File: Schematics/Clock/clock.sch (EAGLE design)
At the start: 13 parts, among them IC1 NE555N

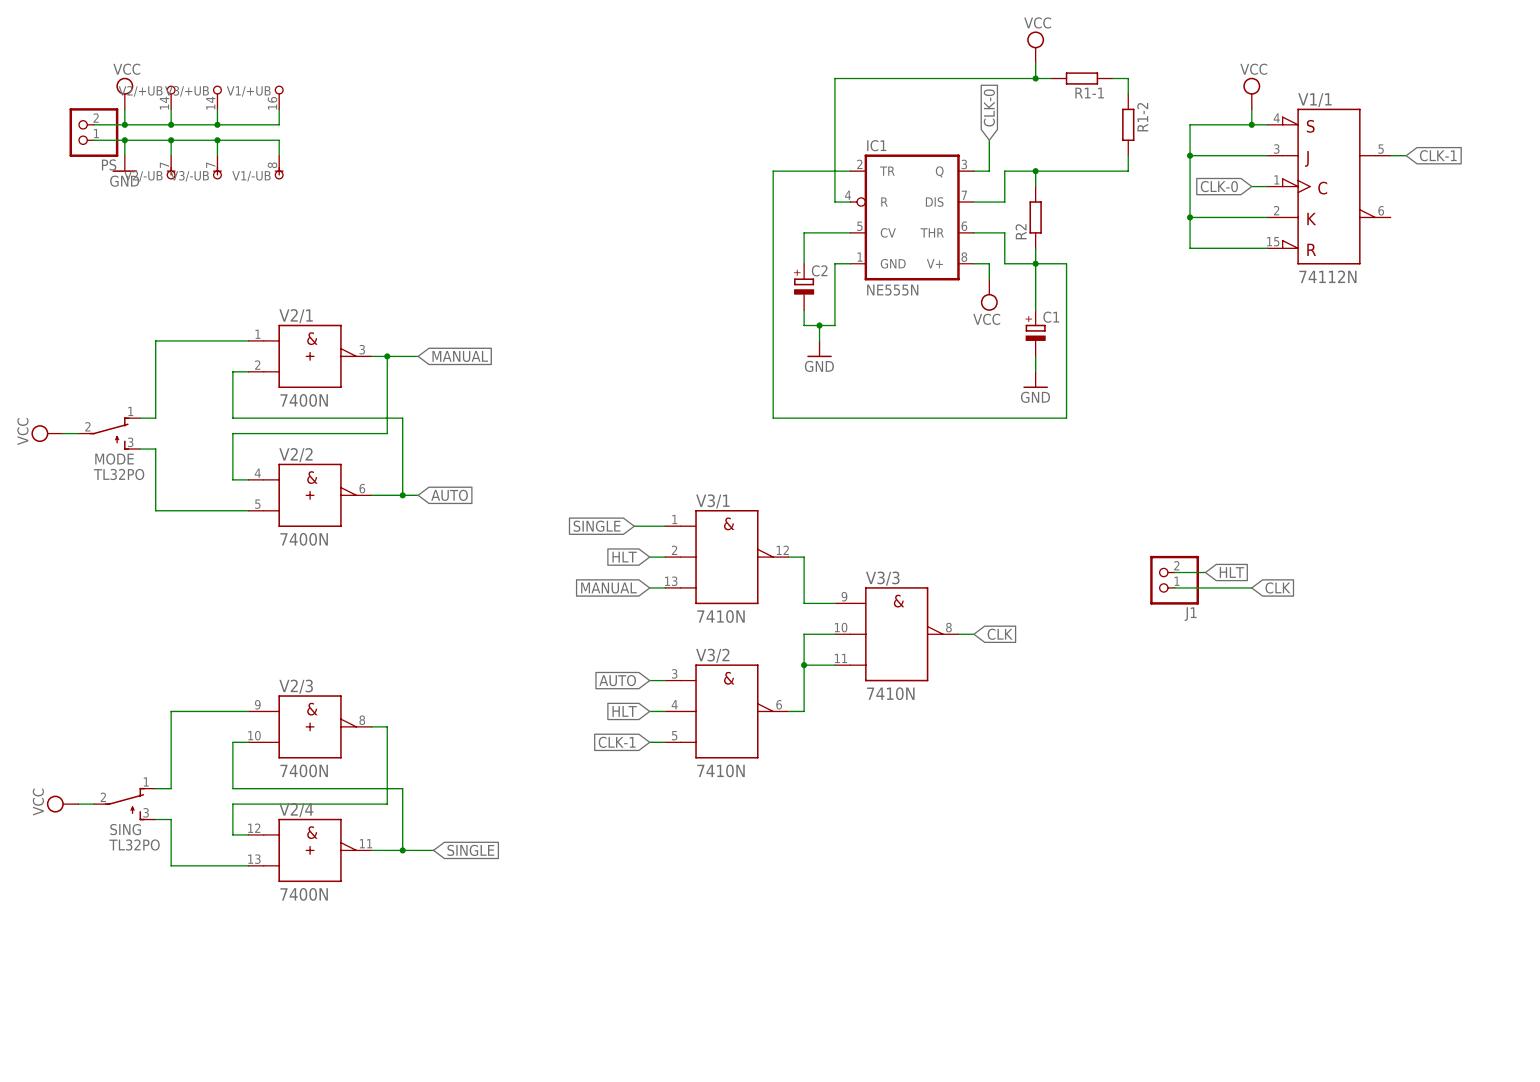
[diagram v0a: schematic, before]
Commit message: Added pull down resisotors to NAND gates. Maybe 'single' will be button.
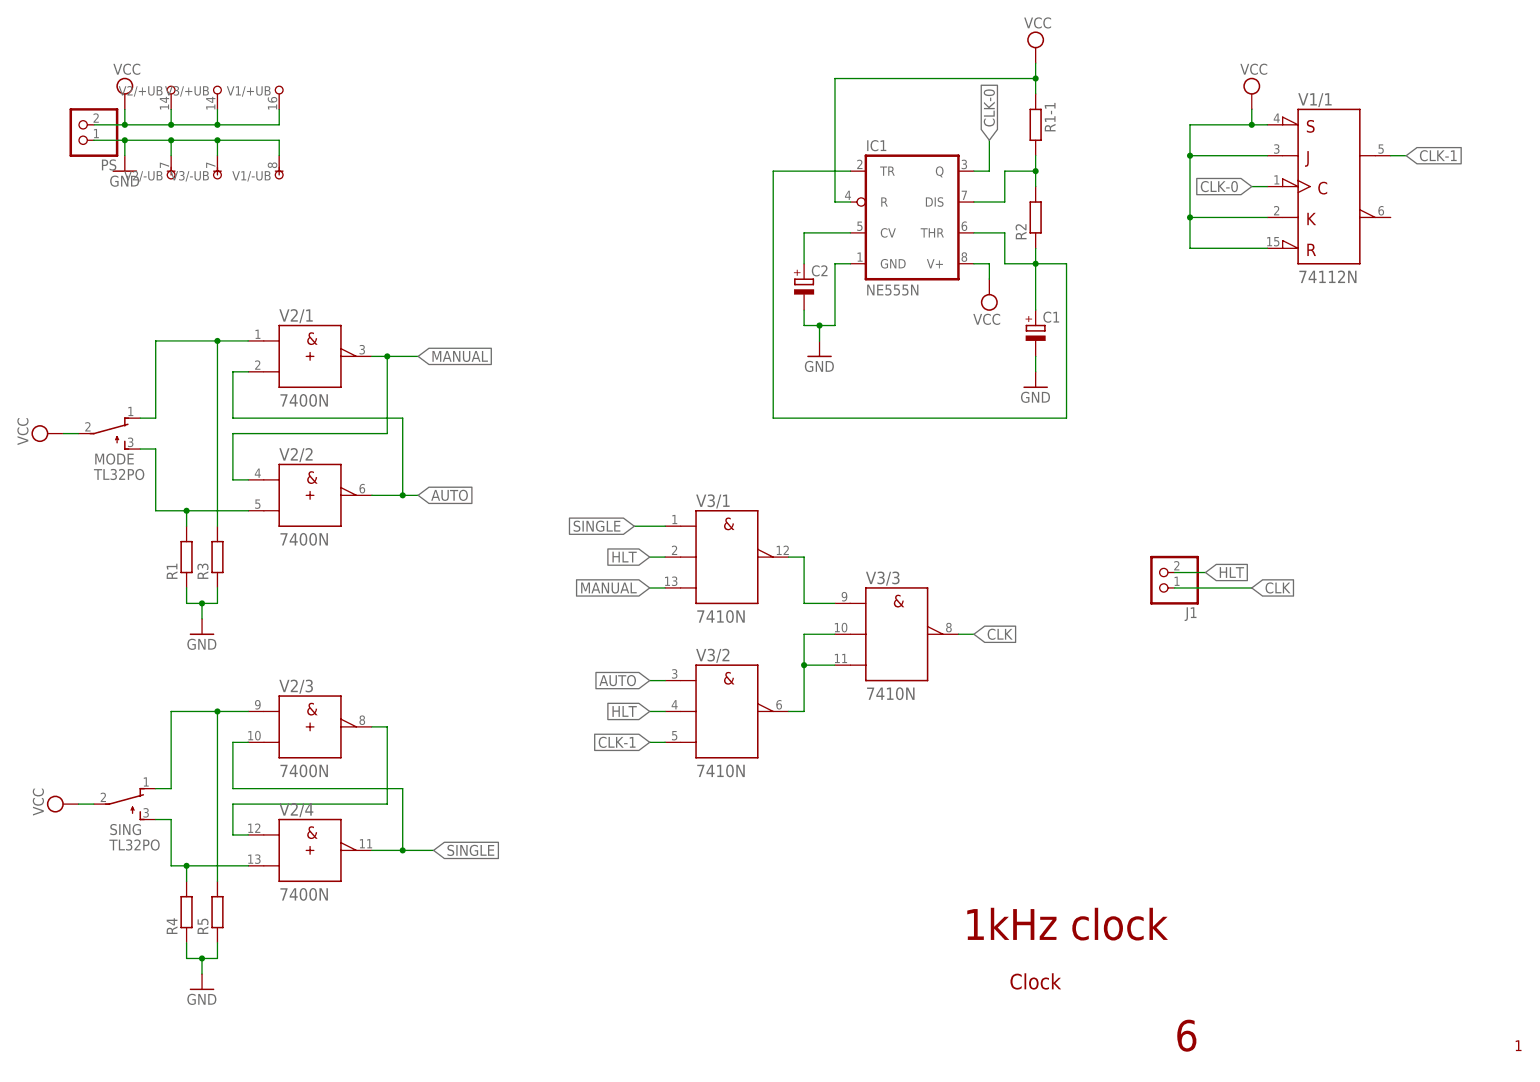
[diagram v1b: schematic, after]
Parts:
- removed R1-2: (no value), rcl:R-EU_0207/10
- added R1, R3, R4, R5: (no value), rcl:R-EU_0204/7
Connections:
- removed net N$4: R1-1.1, R1-2.1
- net GND: now also R1.1, R3.1, R4.1, R5.1
- net N$11: now also R5.2
- net N$12: now also R4.2
- net N$2: now also R1-1.2; no longer R1-2.2
- net N$7: now also R3.2
- net N$8: now also R1.2
- net VCC: now also R1-1.1; no longer R1-1.2
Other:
- note added: "1"
- note added: "1kHz clock"
- note added: "6"
- note added: "Clock"
- moved on the sheet: R1-1
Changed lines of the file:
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@@
 <part name="SUPPLY1" library="supply2" library_urn="urn:adsk.eagle:library:372" deviceset="VCC" device=""/>
 <part name="SUPPLY2" library="supply2" library_urn="urn:adsk.eagle:library:372" deviceset="VCC" device=""/>
-<part name="R1-2" library="rcl" library_urn="urn:adsk.eagle:library:334" deviceset="R-EU_" device="0207/10" package3d_urn="urn:adsk.eagle:package:23491/2"/>
 <part name="V1" library="74ttl-din" library_urn="urn:adsk.eagle:library:84" deviceset="74*112" device="N" package3d_urn="urn:adsk.eagle:package:922/2"/>
 <part name="SUPPLY3" library="supply2" library_urn="urn:adsk.eagle:library:372" deviceset="VCC" device=""/>
@@
 <part name="GND3" library="supply1" library_urn="urn:adsk.eagle:library:371" deviceset="GND" device=""/>
 <part name="J1" library="pinhead" library_urn="urn:adsk.eagle:library:325" deviceset="PINHD-1X2" device="" package3d_urn="urn:adsk.eagle:package:22435/2"/>
+<part name="R1" library="rcl" library_urn="urn:adsk.eagle:library:334" deviceset="R-EU_" device="0204/7" package3d_urn="urn:adsk.eagle:package:23498/2"/>
+<part name="R3" library="rcl" library_urn="urn:adsk.eagle:library:334" deviceset="R-EU_" device="0204/7" package3d_urn="urn:adsk.eagle:package:23498/2"/>
+<part name="R4" library="rcl" library_urn="urn:adsk.eagle:library:334" deviceset="R-EU_" device="0204/7" package3d_urn="urn:adsk.eagle:package:23498/2"/>
+<part name="R5" library="rcl" library_urn="urn:adsk.eagle:library:334" deviceset="R-EU_" device="0204/7" package3d_urn="urn:adsk.eagle:package:23498/2"/>
+<part name="GND4" library="supply1" library_urn="urn:adsk.eagle:library:371" deviceset="GND" device=""/>
+<part name="GND5" library="supply1" library_urn="urn:adsk.eagle:library:371" deviceset="GND" device=""/>
 </parts>
 <sheets>
 <sheet>
 <plain>
+<text x="259.08" y="7.62" size="1.778" layer="94">1</text>
+<text x="203.2" y="7.62" size="5.08" layer="94">6</text>
+<text x="176.022" y="17.78" size="2.54" layer="94">Clock</text>
+<text x="168.402" y="25.908" size="5.08" layer="94">1kHz clock</text>
 </plain>
 <instances>
@@
 <attribute name="LAST_DATE_TIME" x="175.26" y="1.27" size="2.54" layer="94"/>
 <attribute name="SHEET" x="248.92" y="1.27" size="2.54" layer="94"/>
-<attribute name="DRAWING_NAME" x="180.34" y="19.05" size="2.54" layer="94"/>
-</instance>
-<instance part="R1-1" gate="G$1" x="187.96" y="167.64" smashed="yes" rot="R180">
-<attribute name="NAME" x="191.77" y="166.1414" size="1.778" layer="95" rot="R180"/>
-<attribute name="VALUE" x="191.77" y="170.942" size="1.778" layer="96" rot="R180"/>
+</instance>
+<instance part="R1-1" gate="G$1" x="180.34" y="160.02" smashed="yes" rot="R270">
+<attribute name="NAME" x="181.8386" y="163.83" size="1.778" layer="95" rot="R270"/>
+<attribute name="VALUE" x="177.038" y="163.83" size="1.778" layer="96" rot="R270"/>
 </instance>
 <instance part="R2" gate="G$1" x="180.34" y="144.78" smashed="yes" rot="R90">
@@
 <attribute name="VALUE" x="174.625" y="128.905" size="1.778" layer="96" rot="R180"/>
 </instance>
-<instance part="R1-2" gate="G$1" x="195.58" y="160.02" smashed="yes" rot="R270">
-<attribute name="NAME" x="197.0786" y="163.83" size="1.778" layer="95" rot="R270"/>
-<attribute name="VALUE" x="192.278" y="163.83" size="1.778" layer="96" rot="R270"/>
-</instance>
 <instance part="V1" gate="/1" x="228.6" y="149.86" smashed="yes">
 <attribute name="NAME" x="223.52" y="163.195" size="2.032" layer="95"/>
@@
 <instance part="V1" gate="/-UB" x="55.88" y="152.4" smashed="yes" rot="R180">
 <attribute name="NAME" x="54.61" y="152.4" size="1.524" layer="95" rot="R180"/>
+</instance>
+<instance part="R1" gate="G$1" x="40.64" y="88.9" smashed="yes" rot="R90">
+<attribute name="NAME" x="39.1414" y="85.09" size="1.778" layer="95" rot="R90"/>
+<attribute name="VALUE" x="43.942" y="85.09" size="1.778" layer="96" rot="R90"/>
+</instance>
+<instance part="R3" gate="G$1" x="45.72" y="88.9" smashed="yes" rot="R90">
+<attribute name="NAME" x="44.2214" y="85.09" size="1.778" layer="95" rot="R90"/>
+<attribute name="VALUE" x="49.022" y="85.09" size="1.778" layer="96" rot="R90"/>
+</instance>
+<instance part="R4" gate="G$1" x="40.64" y="30.48" smashed="yes" rot="R90">
+<attribute name="NAME" x="39.1414" y="26.67" size="1.778" layer="95" rot="R90"/>
+<attribute name="VALUE" x="43.942" y="26.67" size="1.778" layer="96" rot="R90"/>
+</instance>
+<instance part="R5" gate="G$1" x="45.72" y="30.48" smashed="yes" rot="R90">
+<attribute name="NAME" x="44.2214" y="26.67" size="1.778" layer="95" rot="R90"/>
+<attribute name="VALUE" x="49.022" y="26.67" size="1.778" layer="96" rot="R90"/>
+</instance>
+<instance part="GND4" gate="1" x="43.18" y="76.2" smashed="yes">
+<attribute name="VALUE" x="40.64" y="73.66" size="1.778" layer="96"/>
+</instance>
+<instance part="GND5" gate="1" x="43.18" y="17.78" smashed="yes">
+<attribute name="VALUE" x="40.64" y="15.24" size="1.778" layer="96"/>
 </instance>
 </instances>
@@
 <wire x1="175.26" y1="147.32" x2="175.26" y2="152.4" width="0.1524" layer="91"/>
 <wire x1="175.26" y1="152.4" x2="180.34" y2="152.4" width="0.1524" layer="91"/>
-<wire x1="180.34" y1="152.4" x2="195.58" y2="152.4" width="0.1524" layer="91"/>
+<pinref part="R1-1" gate="G$1" pin="2"/>
+<wire x1="180.34" y1="154.94" x2="180.34" y2="152.4" width="0.1524" layer="91"/>
 <junction x="180.34" y="152.4"/>
-<pinref part="R1-2" gate="G$1" pin="2"/>
-<wire x1="195.58" y1="152.4" x2="195.58" y2="154.94" width="0.1524" layer="91"/>
 </segment>
 </net>
@@
 <wire x1="147.32" y1="147.32" x2="147.32" y2="167.64" width="0.1524" layer="91"/>
 <wire x1="147.32" y1="167.64" x2="180.34" y2="167.64" width="0.1524" layer="91"/>
-<pinref part="R1-1" gate="G$1" pin="2"/>
-<wire x1="180.34" y1="167.64" x2="182.88" y2="167.64" width="0.1524" layer="91"/>
 <pinref part="SUPPLY1" gate="G$1" pin="VCC"/>
 <wire x1="180.34" y1="170.18" x2="180.34" y2="167.64" width="0.1524" layer="91"/>
+<pinref part="R1-1" gate="G$1" pin="1"/>
+<wire x1="180.34" y1="165.1" x2="180.34" y2="167.64" width="0.1524" layer="91"/>
 <junction x="180.34" y="167.64"/>
 </segment>
@@
 <junction x="38.1" y="157.48"/>
 </segment>
+<segment>
+<pinref part="R1" gate="G$1" pin="1"/>
+<wire x1="40.64" y1="83.82" x2="40.64" y2="81.28" width="0.1524" layer="91"/>
+<wire x1="40.64" y1="81.28" x2="43.18" y2="81.28" width="0.1524" layer="91"/>
+<pinref part="R3" gate="G$1" pin="1"/>
+<wire x1="43.18" y1="81.28" x2="45.72" y2="81.28" width="0.1524" layer="91"/>
+<wire x1="45.72" y1="81.28" x2="45.72" y2="83.82" width="0.1524" layer="91"/>
+<pinref part="GND4" gate="1" pin="GND"/>
+<wire x1="43.18" y1="78.74" x2="43.18" y2="81.28" width="0.1524" layer="91"/>
+<junction x="43.18" y="81.28"/>
+</segment>
+<segment>
+<pinref part="R4" gate="G$1" pin="1"/>
+<wire x1="40.64" y1="25.4" x2="40.64" y2="22.86" width="0.1524" layer="91"/>
+<wire x1="40.64" y1="22.86" x2="43.18" y2="22.86" width="0.1524" layer="91"/>
+<pinref part="R5" gate="G$1" pin="1"/>
+<wire x1="43.18" y1="22.86" x2="45.72" y2="22.86" width="0.1524" layer="91"/>
+<wire x1="45.72" y1="22.86" x2="45.72" y2="25.4" width="0.1524" layer="91"/>
+<pinref part="GND5" gate="1" pin="GND"/>
+<wire x1="43.18" y1="20.32" x2="43.18" y2="22.86" width="0.1524" layer="91"/>
+<junction x="43.18" y="22.86"/>
+</segment>
 </net>
 <net name="CLK-0" class="0">
@@
 <wire x1="218.44" y1="149.86" x2="215.9" y2="149.86" width="0.1524" layer="91"/>
 <label x="215.9" y="149.86" size="1.778" layer="95" rot="R180" xref="yes"/>
-</segment>
-</net>
-<net name="N$4" class="0">
-<segment>
-<pinref part="R1-2" gate="G$1" pin="1"/>
-<wire x1="195.58" y1="165.1" x2="195.58" y2="167.64" width="0.1524" layer="91"/>
-<pinref part="R1-1" gate="G$1" pin="1"/>
-<wire x1="195.58" y1="167.64" x2="193.04" y2="167.64" width="0.1524" layer="91"/>
 </segment>
 </net>
@@
 <wire x1="33.02" y1="111.76" x2="35.56" y2="111.76" width="0.1524" layer="91"/>
 <wire x1="35.56" y1="111.76" x2="35.56" y2="124.46" width="0.1524" layer="91"/>
-<wire x1="35.56" y1="124.46" x2="50.8" y2="124.46" width="0.1524" layer="91"/>
+<wire x1="35.56" y1="124.46" x2="45.72" y2="124.46" width="0.1524" layer="91"/>
+<pinref part="R3" gate="G$1" pin="2"/>
+<wire x1="45.72" y1="124.46" x2="50.8" y2="124.46" width="0.1524" layer="91"/>
+<wire x1="45.72" y1="93.98" x2="45.72" y2="124.46" width="0.1524" layer="91"/>
+<junction x="45.72" y="124.46"/>
 </segment>
 </net>
@@
 <wire x1="33.02" y1="106.68" x2="35.56" y2="106.68" width="0.1524" layer="91"/>
 <wire x1="35.56" y1="106.68" x2="35.56" y2="96.52" width="0.1524" layer="91"/>
-<wire x1="35.56" y1="96.52" x2="50.8" y2="96.52" width="0.1524" layer="91"/>
+<wire x1="35.56" y1="96.52" x2="40.64" y2="96.52" width="0.1524" layer="91"/>
+<pinref part="R1" gate="G$1" pin="2"/>
+<wire x1="40.64" y1="96.52" x2="50.8" y2="96.52" width="0.1524" layer="91"/>
+<wire x1="40.64" y1="93.98" x2="40.64" y2="96.52" width="0.1524" layer="91"/>
+<junction x="40.64" y="96.52"/>
 </segment>
 </net>
@@
 <wire x1="38.1" y1="50.8" x2="38.1" y2="63.5" width="0.1524" layer="91"/>
 <pinref part="V2" gate="/3" pin="A"/>
-<wire x1="38.1" y1="63.5" x2="50.8" y2="63.5" width="0.1524" layer="91"/>
+<wire x1="38.1" y1="63.5" x2="45.72" y2="63.5" width="0.1524" layer="91"/>
+<pinref part="R5" gate="G$1" pin="2"/>
+<wire x1="45.72" y1="63.5" x2="50.8" y2="63.5" width="0.1524" layer="91"/>
+<wire x1="45.72" y1="35.56" x2="45.72" y2="63.5" width="0.1524" layer="91"/>
+<junction x="45.72" y="63.5"/>
 </segment>
 </net>
@@
 <wire x1="38.1" y1="45.72" x2="38.1" y2="38.1" width="0.1524" layer="91"/>
 <pinref part="V2" gate="/4" pin="B"/>
-<wire x1="38.1" y1="38.1" x2="50.8" y2="38.1" width="0.1524" layer="91"/>
-</segment>
-</net>
+<wire x1="38.1" y1="38.1" x2="40.64" y2="38.1" width="0.1524" layer="91"/>
+<pinref part="R4" gate="G$1" pin="2"/>
+<wire x1="40.64" y1="38.1" x2="50.8" y2="38.1" width="0.1524" layer="91"/>
+<wire x1="40.64" y1="35.56" x2="40.64" y2="38.1" width="0.1524" layer="91"/>
+<junction x="40.64" y="38.1"/>
+</segment>
+</net>
